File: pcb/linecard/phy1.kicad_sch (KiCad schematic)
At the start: 32 parts, among them J6 XILINX_JTAG, J7 SMPM, J8 SMPM, U10 VSC8512, U60 SIT9121AC-2B2-33E125.000000

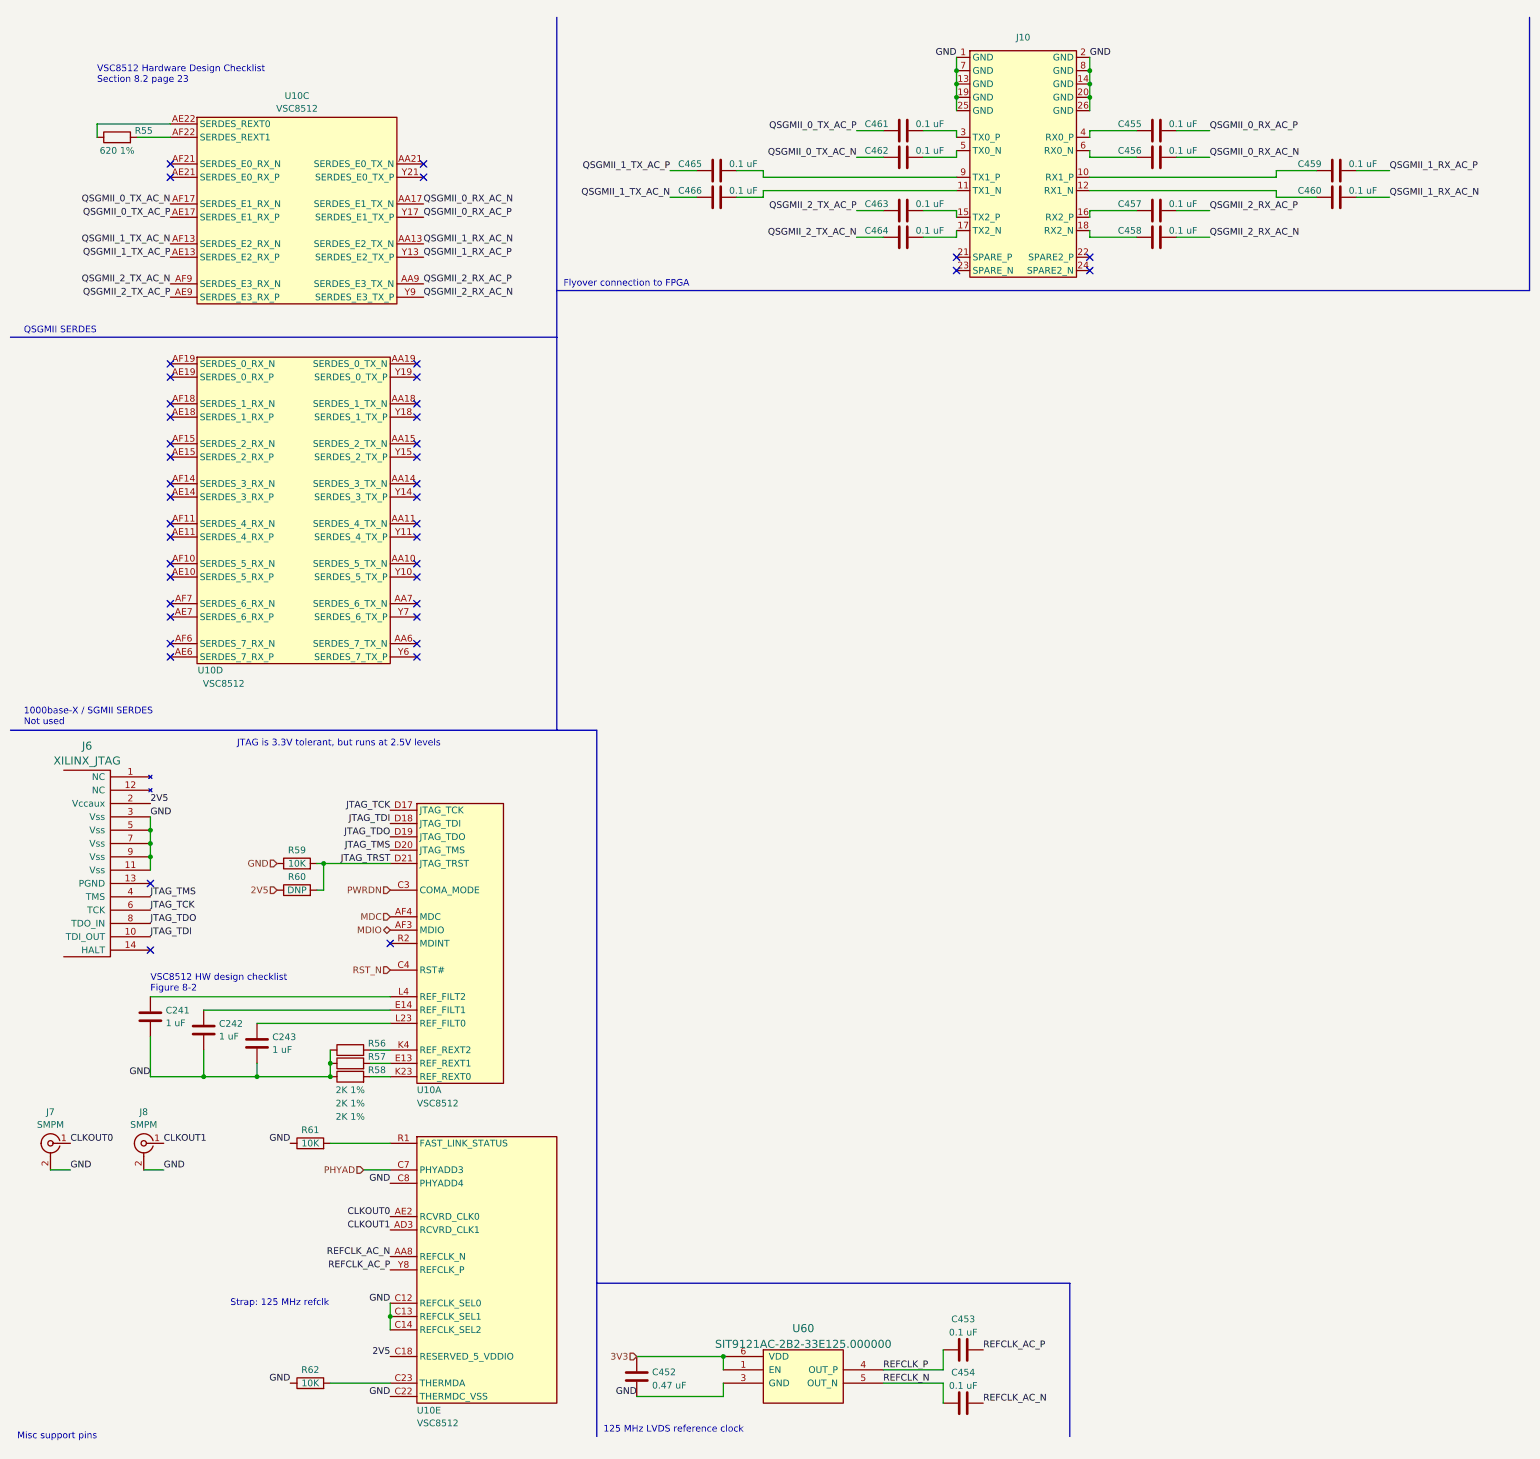
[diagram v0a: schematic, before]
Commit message: Finished initial schematic of line card
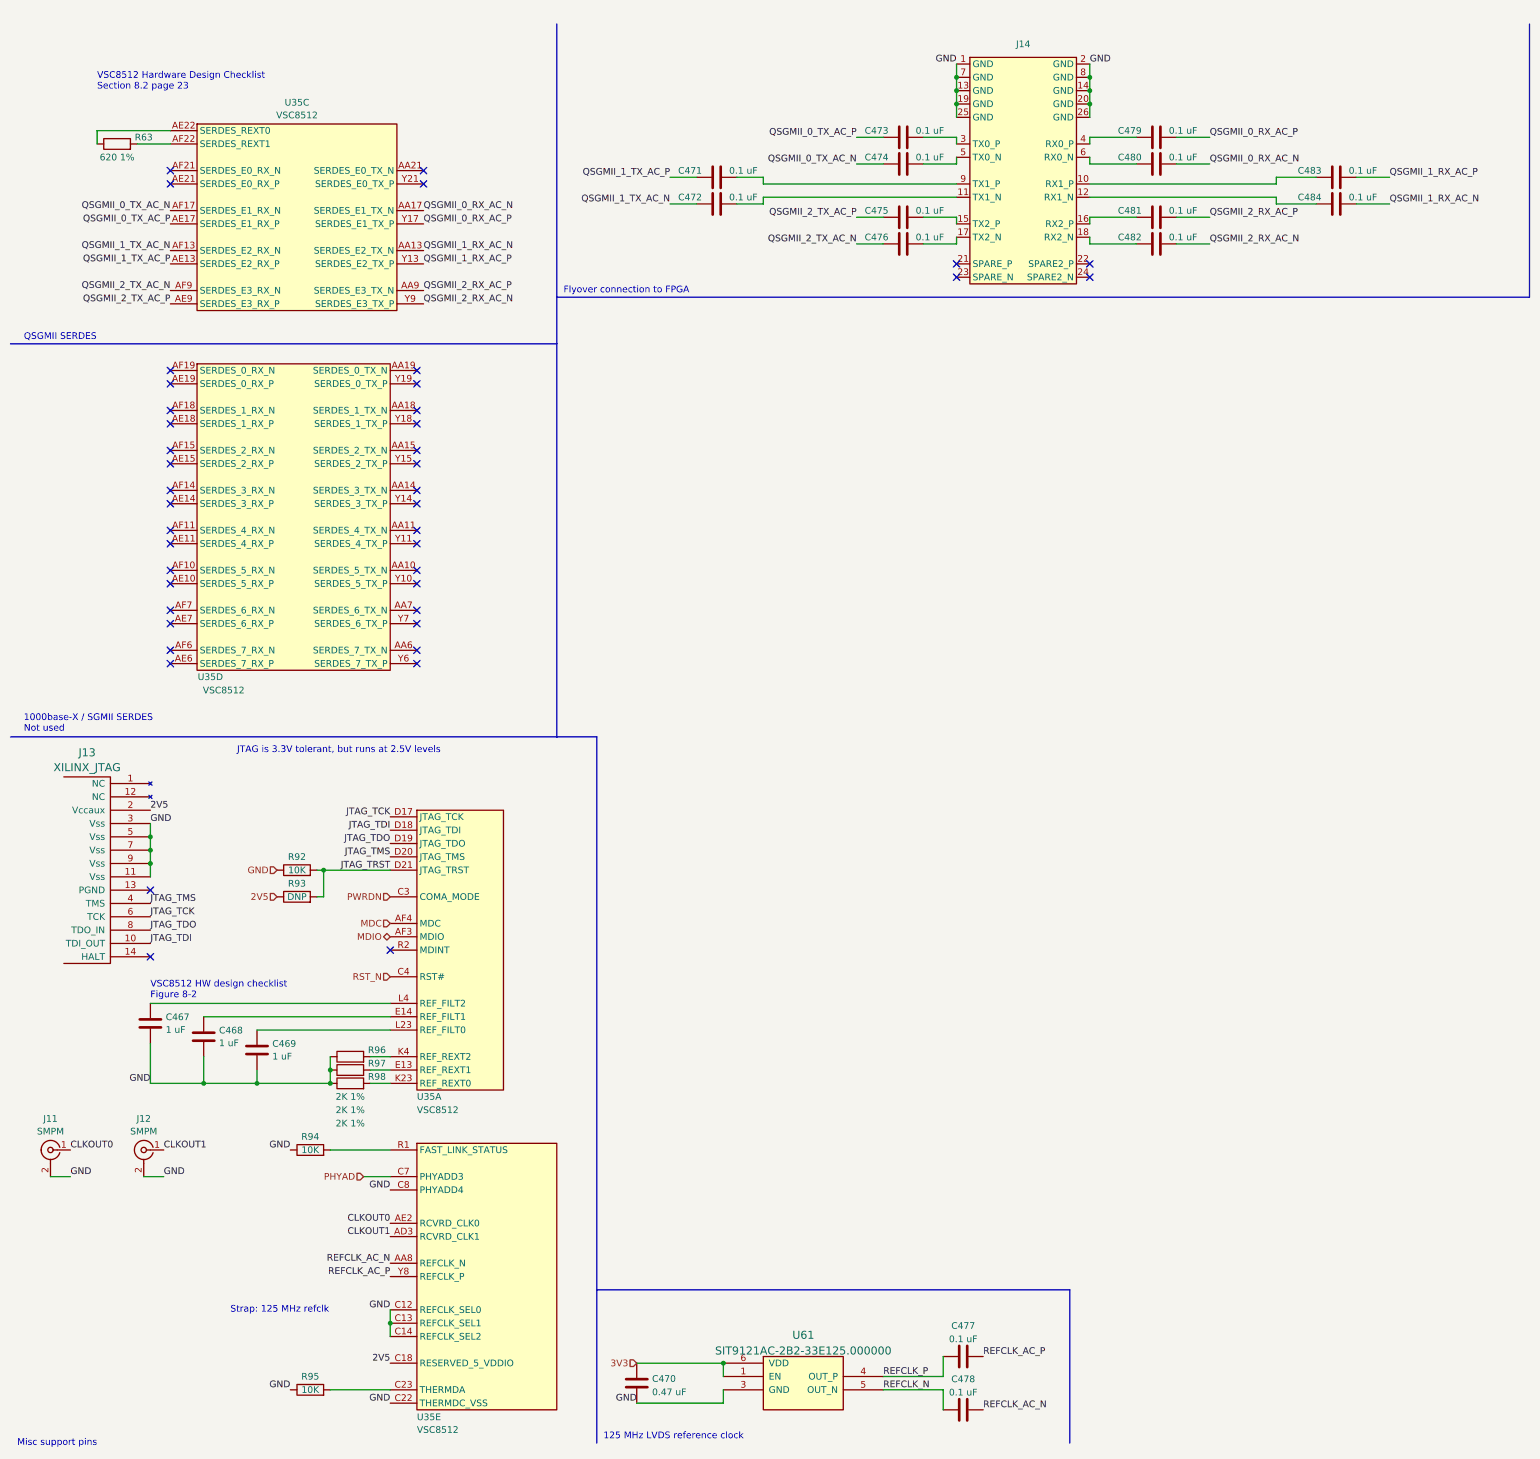
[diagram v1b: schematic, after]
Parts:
- removed C241, C242, C243: 1 uF, azonenberg_pcb:EIA_0402_CAP_NOSILK, symbol device:C
- removed C452: 0.47 uF, azonenberg_pcb:EIA_0402_CAP_NOSILK, symbol device:C
- removed C453, C454, C455, C456, C457, C458, C459, C460, C461, C462, C463, C464, C465, C466: 0.1 uF, azonenberg_pcb:EIA_0402_CAP_NOSILK, symbol device:C
- removed J10: ~, symbol special-azonenberg:CONN_LATENTRED_LINECARD_HS_DEVICE
- removed J6: XILINX_JTAG, azonenberg_pcb:XILINX_JTAG_PTH_MOLEX_0878311420, symbol xilinx-azonenberg:XILINX_JTAG
- removed J7, J8: SMPM, azonenberg_pcb:CONN_SMPM_AMPHENOL_C925-197J-51PT, symbol conn:CONN_COAXIAL
- removed R55: 620 1%, azonenberg_pcb:EIA_0402_RES_NOSILK, symbol device:R
- removed R56, R57, R58: 2K 1%, azonenberg_pcb:EIA_0402_RES_NOSILK, symbol device:R
- removed R59, R61, R62: 10K, azonenberg_pcb:EIA_0402_RES_NOSILK, symbol device:R
- removed R60: DNP, azonenberg_pcb:EIA_0402_RES_NOSILK, symbol device:R
- removed U10: VSC8512, azonenberg_pcb:BGA_676_27x27_FULLARRAY_1MM_FFG676, symbol microchip-azonenberg:VSC8512
- removed U60: SIT9121AC-2B2-33E125.000000, azonenberg_pcb:OSCILLATOR_LVDS_3.2x2.5, symbol osc-azonenberg:OSC_LVDS_NOPAD
- added C467, C468, C469: 1 uF, azonenberg_pcb:EIA_0402_CAP_NOSILK, symbol device:C
- added C470: 0.47 uF, azonenberg_pcb:EIA_0402_CAP_NOSILK, symbol device:C
- added C471, C472, C473, C474, C475, C476, C477, C478, C479, C480, C481, C482, C483, C484: 0.1 uF, azonenberg_pcb:EIA_0402_CAP_NOSILK, symbol device:C
- added J11, J12: SMPM, azonenberg_pcb:CONN_SMPM_AMPHENOL_C925-197J-51PT, symbol conn:CONN_COAXIAL
- added J13: XILINX_JTAG, azonenberg_pcb:XILINX_JTAG_PTH_MOLEX_0878311420, symbol xilinx-azonenberg:XILINX_JTAG
- added J14: ~, symbol special-azonenberg:CONN_LATENTRED_LINECARD_HS_DEVICE
- added R63: 620 1%, azonenberg_pcb:EIA_0402_RES_NOSILK, symbol device:R
- added R92, R94, R95: 10K, azonenberg_pcb:EIA_0402_RES_NOSILK, symbol device:R
- added R93: DNP, azonenberg_pcb:EIA_0402_RES_NOSILK, symbol device:R
- added R96, R97, R98: 2K 1%, azonenberg_pcb:EIA_0402_RES_NOSILK, symbol device:R
- added U35: VSC8512, azonenberg_pcb:BGA_676_27x27_FULLARRAY_1MM_FFG676, symbol microchip-azonenberg:VSC8512
- added U61: SIT9121AC-2B2-33E125.000000, azonenberg_pcb:OSCILLATOR_LVDS_3.2x2.5, symbol osc-azonenberg:OSC_LVDS_NOPAD
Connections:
- net 2V5: now also J13.2 (Vccaux), R93.1, U35.C18 (RESERVED_5_VDDIO)
- net 3V3: now also C470.1, U61.1 (EN), U61.6 (VDD)
- net CLKOUT0: now also J11.1 (In), U35.AE2 (RCVRD_CLK0)
- net CLKOUT1: now also J12.1 (In), U35.AD3 (RCVRD_CLK1)
- net GND: now also C467.2, C468.2, C469.2, C470.2, J11.2 (Ext), J12.2 (Ext), J13.11 (Vss), J13.3 (Vss), J13.5 (Vss), J13.7 (Vss), J13.9 (Vss), J14.1 (GND), J14.13 (GND), J14.14 (GND), J14.19 (GND), J14.2 (GND), J14.20 (GND), J14.25 (GND), J14.26 (GND), J14.7 (GND), J14.8 (GND), R92.1, R94.1, R95.1, R96.1, R97.1, R98.1, U35.C12 (REFCLK_SEL0), U35.C13 (REFCLK_SEL1), U35.C14 (REFCLK_SEL2), U35.C22 (THERMDC_VSS), U35.C8 (PHYADD4), U61.3 (GND)
- net JTAG_TCK: now also J13.6 (TCK), U35.D17 (JTAG_TCK)
- net JTAG_TDI: now also J13.10 (TDI_OUT), U35.D18 (JTAG_TDI)
- net JTAG_TDO: now also J13.8 (TDO_IN), U35.D19 (JTAG_TDO)
- net JTAG_TMS: now also J13.4 (TMS), U35.D20 (JTAG_TMS)
- net JTAG_TRST: now also R92.2, R93.2, U35.D21 (JTAG_TRST)
- net MDC: now also U35.AF4 (MDC)
- net MDIO: now also U35.AF3 (MDIO)
- net PHYAD: now also U35.C7 (PHYADD3)
- net PWRDN: now also U35.C3 (COMA_MODE)
- net QSGMII_0_RX_AC_N: now also C480.2, U35.AA17 (SERDES_E1_TX_N)
- net QSGMII_0_RX_AC_P: now also C479.2, U35.Y17 (SERDES_E1_TX_P)
- net QSGMII_0_TX_AC_N: now also C474.1, U35.AF17 (SERDES_E1_RX_N)
- net QSGMII_0_TX_AC_P: now also C473.1, U35.AE17 (SERDES_E1_RX_P)
- net QSGMII_1_RX_AC_N: now also C484.2, U35.AA13 (SERDES_E2_TX_N)
- net QSGMII_1_RX_AC_P: now also C483.2, U35.Y13 (SERDES_E2_TX_P)
- net QSGMII_1_TX_AC_N: now also C472.1, U35.AF13 (SERDES_E2_RX_N)
- net QSGMII_1_TX_AC_P: now also C471.1, U35.AE13 (SERDES_E2_RX_P)
- net QSGMII_2_RX_AC_N: now also C482.2, U35.Y9 (SERDES_E3_TX_P)
- net QSGMII_2_RX_AC_P: now also C481.2, U35.AA9 (SERDES_E3_TX_N)
- net QSGMII_2_TX_AC_N: now also C476.1, U35.AF9 (SERDES_E3_RX_N)
- net QSGMII_2_TX_AC_P: now also C475.1, U35.AE9 (SERDES_E3_RX_P)
- net REFCLK_AC_N: now also C478.2, U35.AA8 (REFCLK_N)
- net REFCLK_AC_P: now also C477.2, U35.Y8 (REFCLK_P)
- net REFCLK_N: now also C478.1, U61.5 (OUT_N)
- net REFCLK_P: now also C477.1, U61.4 (OUT_P)
- net RST_N: now also U35.C4 (RST#)
- new net: C484.1, J14.12 (RX1_N)
- new net: C482.1, J14.18 (RX2_N)
- new net: R94.2, U35.R1 (FAST_LINK_STATUS)
- new net: R95.2, U35.C23 (THERMDA)
- new net: C480.1, J14.6 (RX0_N)
- new net: C479.1, J14.4 (RX0_P)
- new net: R97.2, U35.E13 (REF_REXT1)
- new net: C468.1, U35.E14 (REF_FILT1)
- new net: R98.2, U35.K23 (REF_REXT0)
- new net: R96.2, U35.K4 (REF_REXT2)
- new net: C469.1, U35.L23 (REF_FILT0)
- new net: C467.1, U35.L4 (REF_FILT2)
- new net: C471.2, J14.9 (TX1_P)
- new net: C476.2, J14.17 (TX2_N)
- new net: C472.2, J14.11 (TX1_N)
- new net: C475.2, J14.15 (TX2_P)
- new net: C483.1, J14.10 (RX1_P)
- new net: C473.2, J14.3 (TX0_P)
- new net: C481.1, J14.16 (RX2_P)
- new net: C474.2, J14.5 (TX0_N)
- new net: R63.1, U35.AE22 (SERDES_REXT0)
- new net: R63.2, U35.AF22 (SERDES_REXT1)

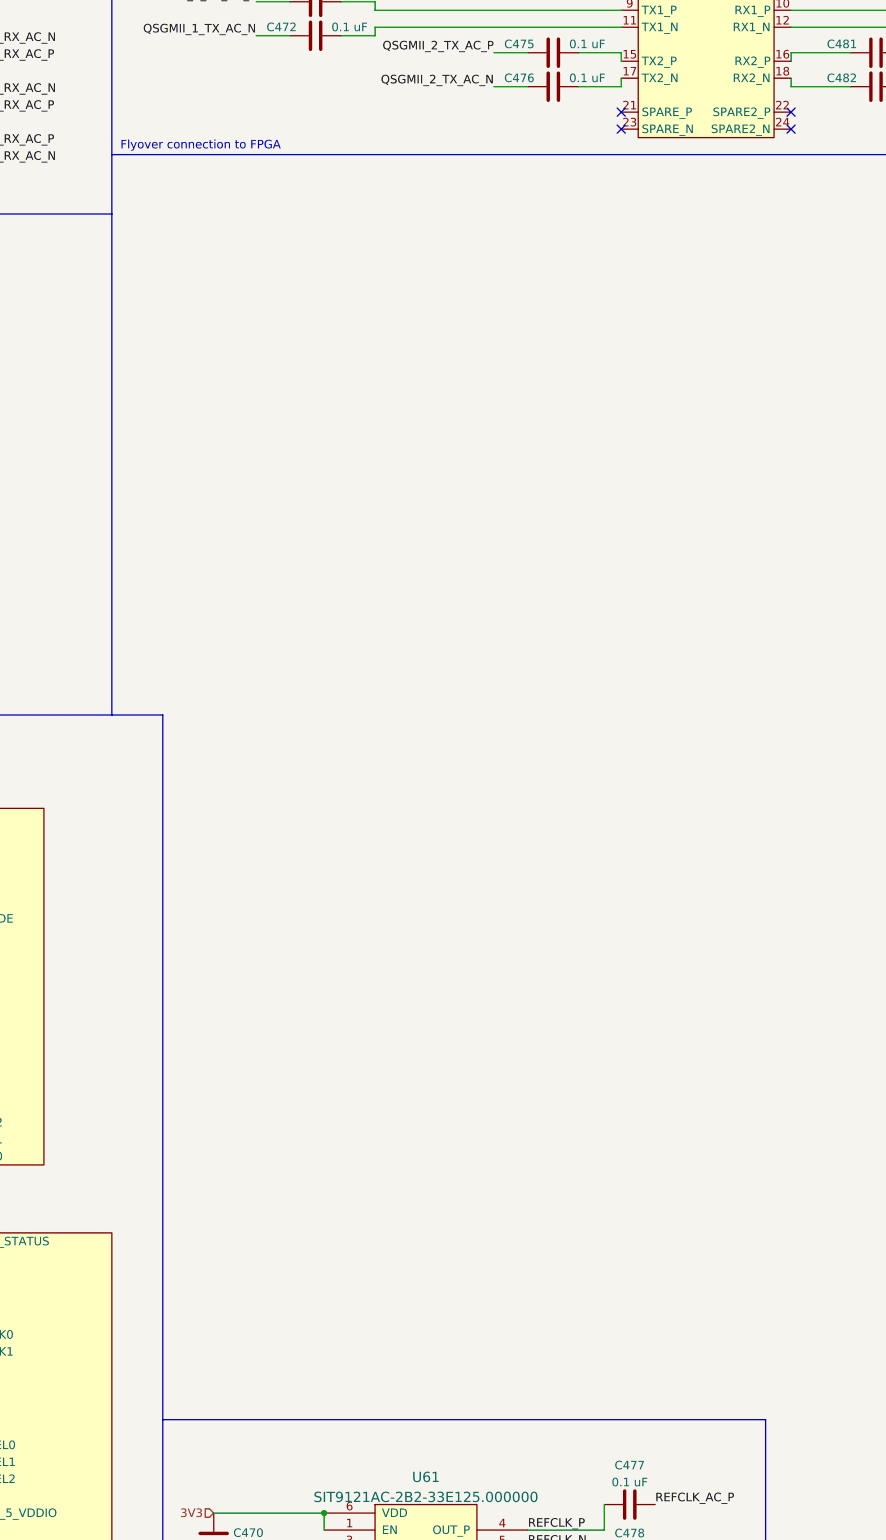
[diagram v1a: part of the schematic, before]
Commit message: Added heatsink, some silkscreen logos, mounting holes, and ground clips
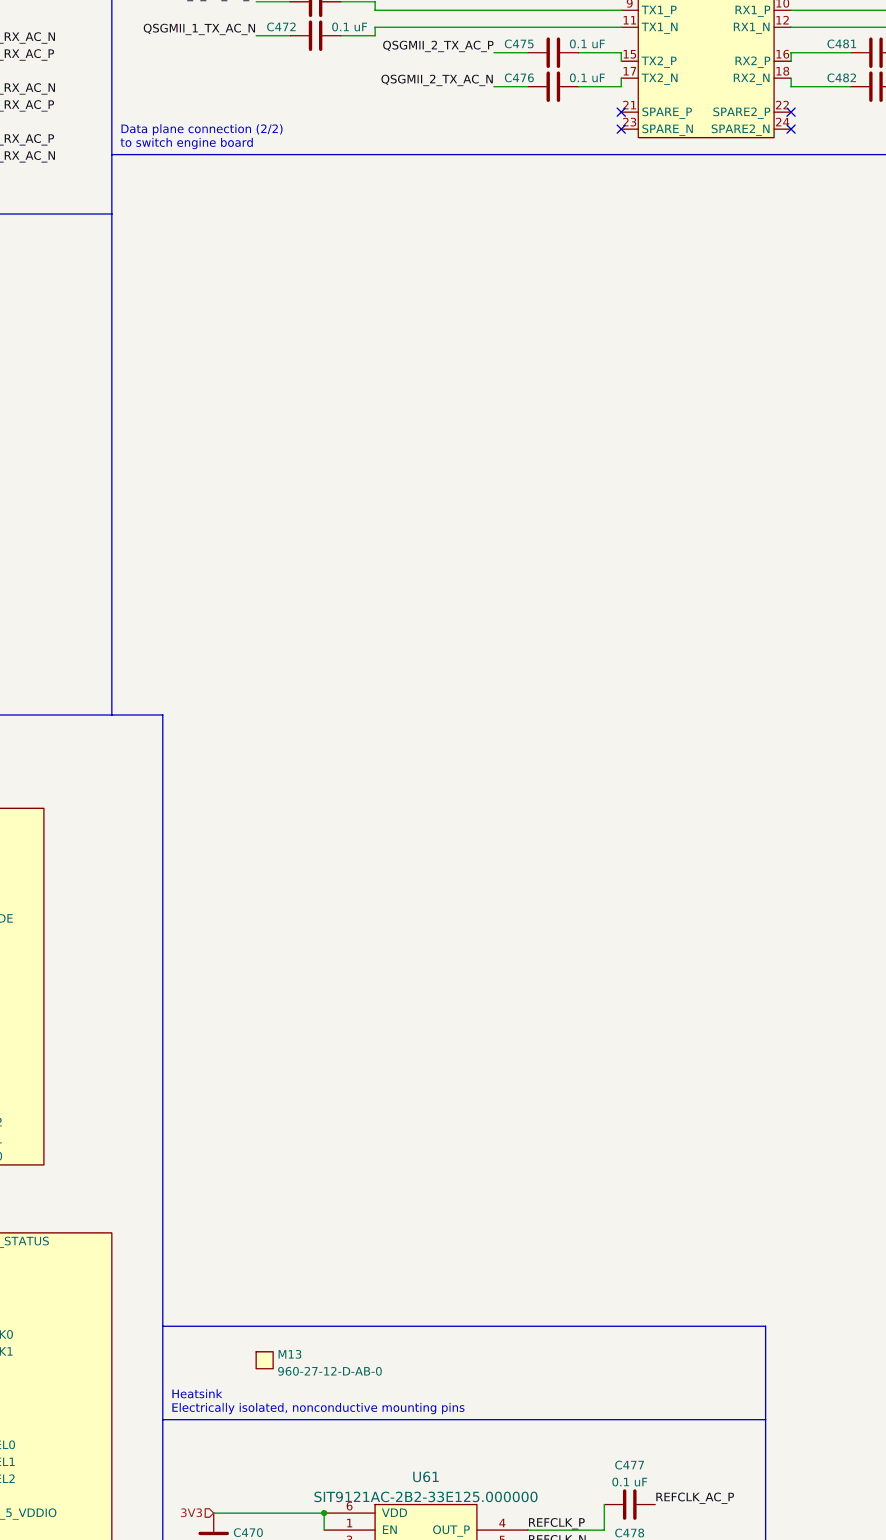
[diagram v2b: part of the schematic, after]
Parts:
- added M13: 960-27-12-D-AB-0, azonenberg_pcb:HEATSINK_WAKEFIELDVETTE_960-27-12-D-AB-0, symbol special-azonenberg:MECHANICAL
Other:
- note added: "Data plane connection (2/2) to switch engine board"
- note added: "Heatsink Electrically isolated, nonconductive mounting pins"
- note removed: "Flyover connection to FPGA"
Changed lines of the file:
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@@
 		)
 	)
+	(polyline
+		(pts
+			(xy 214.63 241.3) (xy 124.46 241.3)
+		)
+		(stroke
+			(width 0)
+			(type default)
+		)
+	)
 	(wire
 		(pts
@@
 		)
 	)
+	(polyline
+		(pts
+			(xy 214.63 241.3) (xy 214.63 255.27)
+		)
+		(stroke
+			(width 0)
+			(type default)
+		)
+	)
 	(wire
 		(pts
@@
 		)
 	)
+	(text "Data plane connection (2/2)\nto switch engine board"
+		(exclude_from_sim no)
+		(at 118.11 63.5 0)
+		(effects
+			(font
+				(size 1.27 1.27)
+			)
+			(justify left)
+		)
+	)
 	(text "QSGMII SERDES"
 		(exclude_from_sim no)
@@
 		)
 	)
-	(text "Flyover connection to FPGA"
+	(text "VSC8512 Hardware Design Checklist\nSection 8.2 page 23"
 		(exclude_from_sim no)
-		(at 118.11 64.77 0)
+		(at 29.21 26.67 0)
 		(effects
 			(font
 				(size 1.27 1.27)
 			)
-			(justify left)
+			(justify left bottom)
 		)
 	)
-	(text "VSC8512 Hardware Design Checklist\nSection 8.2 page 23"
+	(text "Heatsink\nElectrically isolated, nonconductive mounting pins"
 		(exclude_from_sim no)
-		(at 29.21 26.67 0)
+		(at 125.73 252.73 0)
 		(effects
 			(font
 				(size 1.27 1.27)
 			)
-			(justify left bottom)
+			(justify left)
 		)
 	)
@@
 					(unit 1)
 				)
+			)
+		)
+	)
+	(symbol
+		(lib_id "special-azonenberg:MECHANICAL")
+		(at 138.43 246.38 0)
+		(unit 1)
+		(exclude_from_sim no)
+		(in_bom yes)
+		(on_board yes)
+		(dnp no)
+		(property "Reference" "M13"
+			(at 141.605 245.5453 0)
+			(effects
+				(font
+					(size 1.27 1.27)
+				)
+				(justify left)
+			)
+		)
+		(property "Value" "960-27-12-D-AB-0"
+			(at 141.605 248.0822 0)
+			(effects
+				(font
+					(size 1.27 1.27)
+				)
+				(justify left)
+			)
+		)
+		(property "Footprint" "azonenberg_pcb:HEATSINK_WAKEFIELDVETTE_960-27-12-D-AB-0"
+			(at 138.43 246.38 0)
+			(effects
+				(font
+					(size 1.27 1.27)
+				)
+				(hide yes)
+			)
+		)
+		(property "Datasheet" ""
+			(at 138.43 246.38 0)
+			(effects
+				(font
+					(size 1.27 1.27)
+				)
+				(hide yes)
+			)
+		)
+		(property "Description" ""
+			(at 138.43 246.38 0)
+			(effects
+				(font
+					(size 1.27 1.27)
+				)
+				(hide yes)
+			)
+		)
+		(instances
+			(project "linecard"
+				(path "/a55ad1ec-4cad-4d06-8b73-31c98dcc1d79/8f3187c1-80c7-4c27-89ce-e62a99a47325"
+					(reference "M13")
+					(unit 1)
+				)
